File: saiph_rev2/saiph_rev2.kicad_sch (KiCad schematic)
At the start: 205 parts, among them SW1 SW_PUSH, SW10 SW_PUSH, SW100 SW_PUSH, SW101 SW_PUSH, SW102 SW_PUSH, SW103 SW_PUSH, SW104 SW_PUSH, SW105 SW_PUSH, SW109 SW_PUSH, SW11 SW_PUSH, SW110 SW_PUSH, SW111 SW_PUSH, SW12 SW_PUSH, SW13 SW_PUSH, SW14 SW_PUSH, SW15 SW_PUSH, SW16 SW_PUSH, SW17 SW_PUSH, SW18 SW_PUSH, SW19 SW_PUSH, SW2 SW_PUSH, SW20 SW_PUSH, SW21 SW_PUSH, SW22 SW_PUSH, SW23 SW_PUSH, SW24 SW_PUSH, SW25 SW_PUSH, SW26 SW_PUSH, SW27 SW_PUSH, SW28 SW_PUSH, SW29 SW_PUSH, SW3 SW_PUSH, SW30 SW_PUSH, SW31 SW_PUSH, SW32 SW_PUSH, SW33 SW_PUSH, SW34 SW_PUSH, SW35 SW_PUSH, SW36 SW_PUSH, SW37 SW_PUSH, SW38 SW_PUSH, SW39 SW_PUSH, SW4 SW_PUSH, SW40 SW_PUSH, SW41 SW_PUSH, SW42 SW_PUSH, SW43 SW_PUSH, SW44 SW_PUSH, SW45 SW_PUSH, SW46 SW_PUSH, SW47 SW_PUSH, SW48 SW_PUSH, SW49 SW_PUSH, SW5 SW_PUSH, SW50 SW_PUSH, SW51 SW_PUSH, SW52 SW_PUSH, SW53 SW_PUSH, SW54 SW_PUSH, SW55 SW_PUSH, SW56 SW_PUSH, SW57 SW_PUSH, SW58 SW_PUSH, SW59 SW_PUSH, SW6 SW_PUSH, SW60 SW_PUSH, SW61 SW_PUSH, SW62 SW_PUSH, SW63 SW_PUSH, SW64 SW_PUSH, SW65 SW_PUSH, SW66 SW_PUSH, SW67 SW_PUSH, SW68 SW_PUSH, SW69 SW_PUSH, SW7 SW_PUSH, SW70 SW_PUSH, SW71 SW_PUSH, SW72 SW_PUSH, SW73 SW_PUSH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

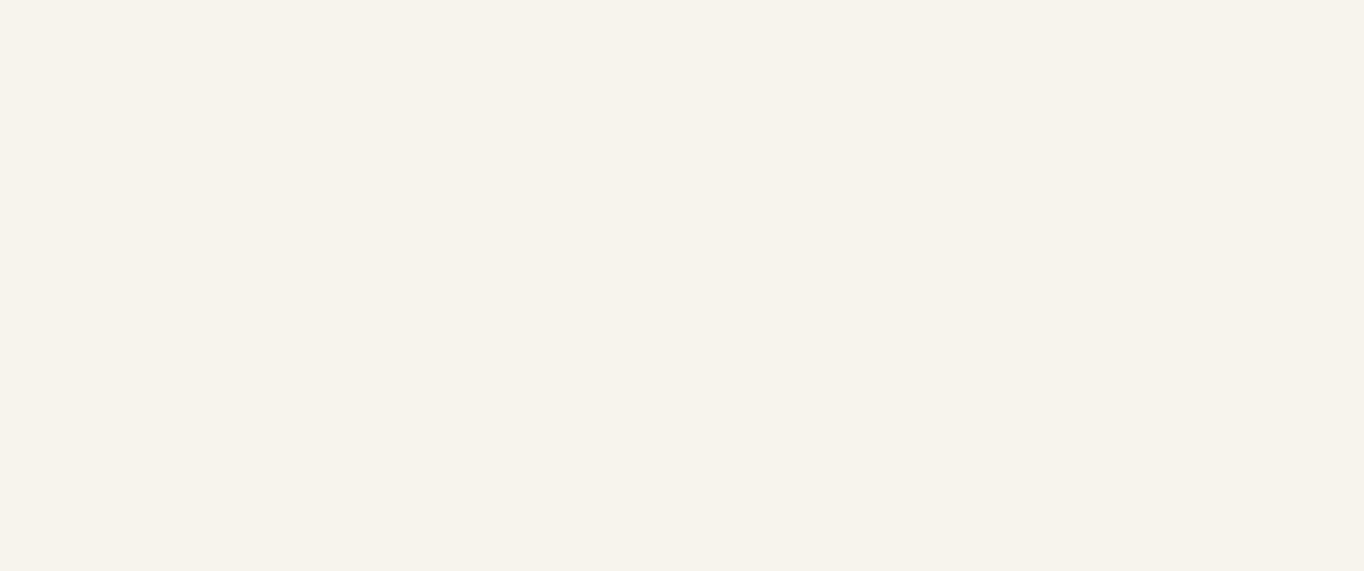
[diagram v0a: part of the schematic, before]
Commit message: add pro micro and usb
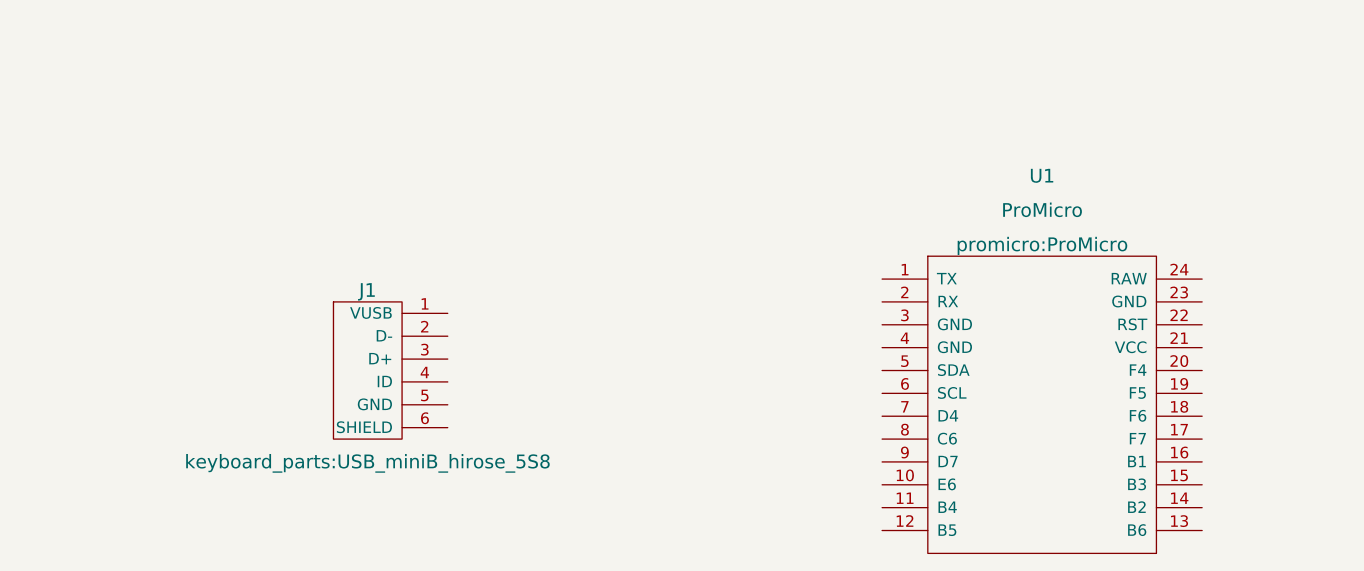
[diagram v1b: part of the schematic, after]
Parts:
- added J1: USB_mini_micro_B, keyboard_parts:USB_miniB_hirose_5S8, symbol keyboard_parts:USB_mini_micro_B
- added U1: ProMicro, promicro:ProMicro, symbol promicro:ProMicro
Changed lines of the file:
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@@
     (pin "2")
+  )
+  (symbol (lib_id "keyboard_parts:USB_mini_micro_B") (at 66.04 191.77 0) (unit 1)
+    (in_bom yes) (on_board yes)
+    (property "Reference" "J1" (id 0) (at 60.96 185.42 0)
+      (effects (font (size 1.524 1.524)))
+    )
+    (property "Value" "USB_mini_micro_B" (id 1) (at 62.23 185.42 0)
+      (effects (font (size 1.524 1.524)) hide)
+    )
+    (property "Footprint" "keyboard_parts:USB_miniB_hirose_5S8" (id 2) (at 60.96 204.47 0)
+      (effects (font (size 1.524 1.524)))
+    )
+    (property "Datasheet" "" (id 3) (at 64.77 191.77 0)
+      (effects (font (size 1.524 1.524)))
+    )
+    (pin "1")
+    (pin "2")
+    (pin "3")
+    (pin "4")
+    (pin "5")
+    (pin "6")
   )
   (symbol (lib_id "Device:LED") (at 26.67 31.75 0) (unit 1)
@@
     (pin "2")
   )
+  (symbol (lib_id "promicro:ProMicro") (at 135.89 203.2 0) (unit 1)
+    (in_bom yes) (on_board yes) (fields_autoplaced)
+    (property "Reference" "U1" (id 0) (at 135.89 172.72 0)
+      (effects (font (size 1.524 1.524)))
+    )
+    (property "Value" "ProMicro" (id 1) (at 135.89 176.53 0)
+      (effects (font (size 1.524 1.524)))
+    )
+    (property "Footprint" "promicro:ProMicro" (id 2) (at 135.89 180.34 0)
+      (effects (font (size 1.524 1.524)))
+    )
+    (property "Datasheet" "" (id 3) (at 138.43 229.87 0)
+      (effects (font (size 1.524 1.524)))
+    )
+    (pin "1")
+    (pin "10")
+    (pin "11")
+    (pin "12")
+    (pin "13")
+    (pin "14")
+    (pin "15")
+    (pin "16")
+    (pin "17")
+    (pin "18")
+    (pin "19")
+    (pin "2")
+    (pin "20")
+    (pin "21")
+    (pin "22")
+    (pin "23")
+    (pin "24")
+    (pin "3")
+    (pin "4")
+    (pin "5")
+    (pin "6")
+    (pin "7")
+    (pin "8")
+    (pin "9")
+  )
   (sheet_instances
     (path "/" (page "1"))
@@
       (reference "D98") (unit 1) (value "D") (footprint "Diodes_ThroughHole:D_DO-35_SOD27_P7.62mm_Horizontal")
     )
+    (path "/3b42597a-f840-489c-a144-f29527fd38e5"
+      (reference "J1") (unit 1) (value "USB_mini_micro_B") (footprint "keyboard_parts:USB_miniB_hirose_5S8")
+    )
     (path "/00000000-0000-0000-0000-000059446b96"
       (reference "SW1") (unit 1) (value "SW_PUSH") (footprint "keyboard_parts:ALPS_PLATE")
@@
       (reference "SW111") (unit 1) (value "SW_PUSH") (footprint "keyboard_parts:ALPS_PLATE_PLATE")
     )
+    (path "/d98210f0-6696-4934-86e8-c5c59831d86a"
+      (reference "U1") (unit 1) (value "ProMicro") (footprint "promicro:ProMicro")
+    )
   )

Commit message: add promicro
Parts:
- added J2: Conn_01x04, Connector_PinHeader_2.54mm:PinHeader_1x04_P2.54mm_Vertical, symbol Connector_Generic:Conn_01x04
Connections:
- net C0: now also U1.12 (B5)
- net C1: now also U1.11 (B4)
- net C2: now also U1.10 (E6)
- net C3: now also U1.9 (D7)
- net C4: now also U1.8 (C6)
- net C5: now also U1.7 (D4)
- net C6: now also U1.6 (SCL)
- net C7: now also U1.20 (F4)
- net C8: now also U1.19 (F5)
- net R0: now also U1.13 (B6)
- net R1: now also U1.14 (B2)
- net R2: now also U1.15 (B3)
- net R3: now also U1.16 (B1)
- net R4: now also U1.17 (F7)
- net R5: now also U1.18 (F6)
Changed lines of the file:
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@@
     (effects (font (size 1.27 1.27)) (justify left bottom))
+  )
+  (hierarchical_label "R0" (shape input) (at 153.67 212.09 0)
+    (effects (font (size 1.524 1.524)) (justify left))
   )
   (hierarchical_label "C0" (shape input) (at 110.49 33.02 90)
     (effects (font (size 1.524 1.524)) (justify left))
   )
+  (hierarchical_label "R3" (shape input) (at 153.67 204.47 0)
+    (effects (font (size 1.524 1.524)) (justify left))
+  )
+  (hierarchical_label "R2" (shape input) (at 153.67 207.01 0)
+    (effects (font (size 1.524 1.524)) (justify left))
+  )
   (hierarchical_label "C7" (shape input) (at 466.09 33.02 90)
     (effects (font (size 1.524 1.524)) (justify left))
   )
+  (hierarchical_label "C2" (shape input) (at 118.11 207.01 180)
+    (effects (font (size 1.524 1.524)) (justify right))
+  )
   (hierarchical_label "R0" (shape input) (at 109.22 45.72 180)
     (effects (font (size 1.524 1.524)) (justify right))
   )
+  (hierarchical_label "C3" (shape input) (at 118.11 204.47 180)
+    (effects (font (size 1.524 1.524)) (justify right))
+  )
   (hierarchical_label "C8" (shape input) (at 516.89 33.02 90)
     (effects (font (size 1.524 1.524)) (justify left))
   )
+  (hierarchical_label "C4" (shape input) (at 118.11 201.93 180)
+    (effects (font (size 1.524 1.524)) (justify right))
+  )
   (hierarchical_label "C2" (shape input) (at 210.82 33.02 90)
     (effects (font (size 1.524 1.524)) (justify left))
@@
     (effects (font (size 1.524 1.524)) (justify left))
   )
+  (hierarchical_label "C0" (shape input) (at 118.11 212.09 180)
+    (effects (font (size 1.524 1.524)) (justify right))
+  )
   (hierarchical_label "R5" (shape input) (at 109.22 134.62 180)
     (effects (font (size 1.524 1.524)) (justify right))
   )
+  (hierarchical_label "C6" (shape input) (at 118.11 196.85 180)
+    (effects (font (size 1.524 1.524)) (justify right))
+  )
+  (hierarchical_label "C7" (shape input) (at 153.67 194.31 0)
+    (effects (font (size 1.524 1.524)) (justify left))
+  )
   (hierarchical_label "R2" (shape input) (at 109.22 81.28 180)
     (effects (font (size 1.524 1.524)) (justify right))
   )
+  (hierarchical_label "R1" (shape input) (at 153.67 209.55 0)
+    (effects (font (size 1.524 1.524)) (justify left))
+  )
+  (hierarchical_label "C1" (shape input) (at 118.11 209.55 180)
+    (effects (font (size 1.524 1.524)) (justify right))
+  )
+  (hierarchical_label "R4" (shape input) (at 153.67 201.93 0)
+    (effects (font (size 1.524 1.524)) (justify left))
+  )
+  (hierarchical_label "R5" (shape input) (at 153.67 199.39 0)
+    (effects (font (size 1.524 1.524)) (justify left))
+  )
   (hierarchical_label "R4" (shape input) (at 109.22 116.84 180)
     (effects (font (size 1.524 1.524)) (justify right))
@@
     (effects (font (size 1.524 1.524)) (justify left))
   )
+  (hierarchical_label "C5" (shape input) (at 118.11 199.39 180)
+    (effects (font (size 1.524 1.524)) (justify right))
+  )
   (hierarchical_label "C5" (shape input) (at 364.49 33.02 90)
+    (effects (font (size 1.524 1.524)) (justify left))
+  )
+  (hierarchical_label "C8" (shape input) (at 153.67 196.85 0)
     (effects (font (size 1.524 1.524)) (justify left))
   )
@@
     (pin "1")
     (pin "2")
+  )
+  (symbol (lib_id "Connector_Generic:Conn_01x04") (at 81.28 193.04 0) (unit 1)
+    (in_bom yes) (on_board yes) (fields_autoplaced)
+    (property "Reference" "J2" (id 0) (at 83.82 193.0399 0)
+      (effects (font (size 1.27 1.27)) (justify left))
+    )
+    (property "Value" "Conn_01x04" (id 1) (at 83.82 195.5799 0)
+      (effects (font (size 1.27 1.27)) (justify left))
+    )
+    (property "Footprint" "Connector_PinHeader_2.54mm:PinHeader_1x04_P2.54mm_Vertical" (id 2) (at 81.28 193.04 0)
+      (effects (font (size 1.27 1.27)) hide)
+    )
+    (property "Datasheet" "~" (id 3) (at 81.28 193.04 0)
+      (effects (font (size 1.27 1.27)) hide)
+    )
+    (pin "1")
+    (pin "2")
+    (pin "3")
+    (pin "4")
   )
   (symbol (lib_id "keyboard_parts:USB_mini_micro_B") (at 66.04 191.77 0) (unit 1)
@@
       (reference "J1") (unit 1) (value "USB_mini_micro_B") (footprint "keyboard_parts:USB_miniB_hirose_5S8")
     )
+    (path "/11831a87-a89a-47da-93c1-04d31768f1fb"
+      (reference "J2") (unit 1) (value "Conn_01x04") (footprint "Connector_PinHeader_2.54mm:PinHeader_1x04_P2.54mm_Vertical")
+    )
     (path "/00000000-0000-0000-0000-000059446b96"

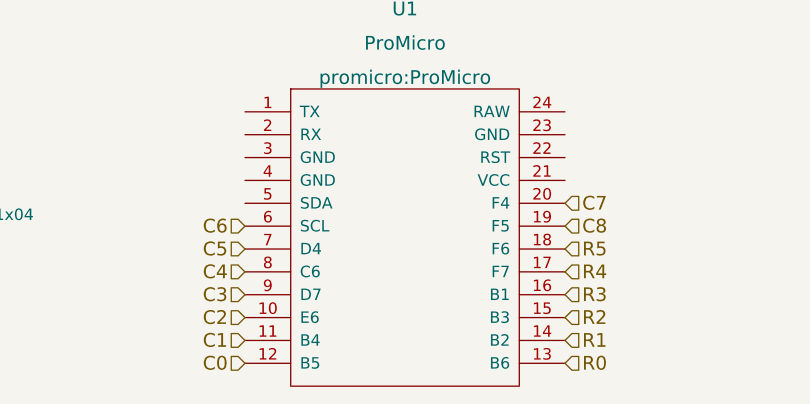
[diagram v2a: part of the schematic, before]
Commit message: change footprints to attempt better fit
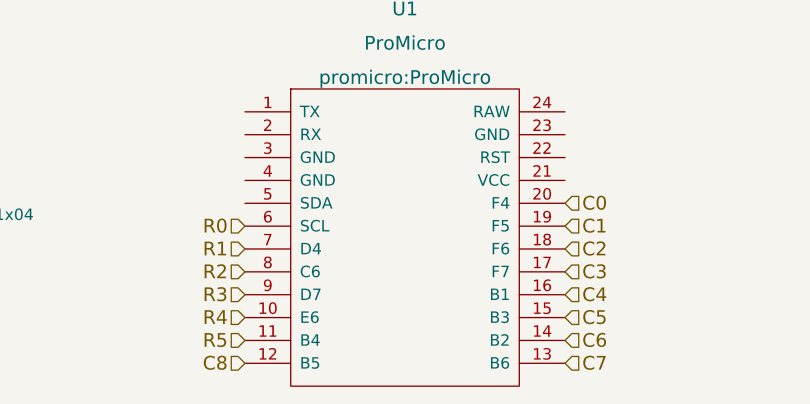
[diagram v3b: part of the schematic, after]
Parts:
- SW75, SW76, SW81, SW82: footprint keyboard_parts:ALPS_PLATE -> custom_parts:ALPS_PLATE_SPRING_PARTIAL
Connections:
- net C0: now also U1.20 (F4); no longer U1.12 (B5)
- net C1: now also U1.19 (F5); no longer U1.11 (B4)
- net C2: now also U1.18 (F6); no longer U1.10 (E6)
- net C3: now also U1.17 (F7); no longer U1.9 (D7)
- net C4: now also U1.16 (B1); no longer U1.8 (C6)
- net C5: now also U1.15 (B3); no longer U1.7 (D4)
- net C6: now also U1.14 (B2); no longer U1.6 (SCL)
- net C7: now also U1.13 (B6); no longer U1.20 (F4)
- net C8: now also U1.12 (B5); no longer U1.19 (F5)
- net R0: now also U1.6 (SCL); no longer U1.13 (B6)
- net R1: now also U1.7 (D4); no longer U1.14 (B2)
- net R2: now also U1.8 (C6); no longer U1.15 (B3)
- net R3: now also U1.9 (D7); no longer U1.16 (B1)
- net R4: now also U1.10 (E6); no longer U1.17 (F7)
- net R5: now also U1.11 (B4); no longer U1.18 (F6)
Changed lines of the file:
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@@
     (effects (font (size 1.27 1.27)) (justify left bottom))
   )
-  (hierarchical_label "R0" (shape input) (at 153.67 212.09 0)
-    (effects (font (size 1.524 1.524)) (justify left))
+  (hierarchical_label "R0" (shape input) (at 118.11 196.85 180)
+    (effects (font (size 1.524 1.524)) (justify right))
   )
   (hierarchical_label "C0" (shape input) (at 110.49 33.02 90)
     (effects (font (size 1.524 1.524)) (justify left))
   )
-  (hierarchical_label "R3" (shape input) (at 153.67 204.47 0)
-    (effects (font (size 1.524 1.524)) (justify left))
-  )
-  (hierarchical_label "R2" (shape input) (at 153.67 207.01 0)
-    (effects (font (size 1.524 1.524)) (justify left))
+  (hierarchical_label "R3" (shape input) (at 118.11 204.47 180)
+    (effects (font (size 1.524 1.524)) (justify right))
+  )
+  (hierarchical_label "R2" (shape input) (at 118.11 201.93 180)
+    (effects (font (size 1.524 1.524)) (justify right))
   )
   (hierarchical_label "C7" (shape input) (at 466.09 33.02 90)
     (effects (font (size 1.524 1.524)) (justify left))
   )
-  (hierarchical_label "C2" (shape input) (at 118.11 207.01 180)
-    (effects (font (size 1.524 1.524)) (justify right))
+  (hierarchical_label "C2" (shape input) (at 153.67 199.39 0)
+    (effects (font (size 1.524 1.524)) (justify left))
   )
   (hierarchical_label "R0" (shape input) (at 109.22 45.72 180)
     (effects (font (size 1.524 1.524)) (justify right))
   )
-  (hierarchical_label "C3" (shape input) (at 118.11 204.47 180)
-    (effects (font (size 1.524 1.524)) (justify right))
+  (hierarchical_label "C3" (shape input) (at 153.67 201.93 0)
+    (effects (font (size 1.524 1.524)) (justify left))
   )
   (hierarchical_label "C8" (shape input) (at 516.89 33.02 90)
     (effects (font (size 1.524 1.524)) (justify left))
   )
-  (hierarchical_label "C4" (shape input) (at 118.11 201.93 180)
-    (effects (font (size 1.524 1.524)) (justify right))
+  (hierarchical_label "C4" (shape input) (at 153.67 204.47 0)
+    (effects (font (size 1.524 1.524)) (justify left))
   )
   (hierarchical_label "C2" (shape input) (at 210.82 33.02 90)
@@
     (effects (font (size 1.524 1.524)) (justify left))
   )
-  (hierarchical_label "C0" (shape input) (at 118.11 212.09 180)
-    (effects (font (size 1.524 1.524)) (justify right))
+  (hierarchical_label "C0" (shape input) (at 153.67 194.31 0)
+    (effects (font (size 1.524 1.524)) (justify left))
   )
   (hierarchical_label "R5" (shape input) (at 109.22 134.62 180)
     (effects (font (size 1.524 1.524)) (justify right))
   )
-  (hierarchical_label "C6" (shape input) (at 118.11 196.85 180)
-    (effects (font (size 1.524 1.524)) (justify right))
-  )
-  (hierarchical_label "C7" (shape input) (at 153.67 194.31 0)
+  (hierarchical_label "C6" (shape input) (at 153.67 209.55 0)
+    (effects (font (size 1.524 1.524)) (justify left))
+  )
+  (hierarchical_label "C7" (shape input) (at 153.67 212.09 0)
     (effects (font (size 1.524 1.524)) (justify left))
   )
@@
     (effects (font (size 1.524 1.524)) (justify right))
   )
-  (hierarchical_label "R1" (shape input) (at 153.67 209.55 0)
+  (hierarchical_label "R1" (shape input) (at 118.11 199.39 180)
+    (effects (font (size 1.524 1.524)) (justify right))
+  )
+  (hierarchical_label "C1" (shape input) (at 153.67 196.85 0)
     (effects (font (size 1.524 1.524)) (justify left))
   )
-  (hierarchical_label "C1" (shape input) (at 118.11 209.55 180)
+  (hierarchical_label "R4" (shape input) (at 118.11 207.01 180)
     (effects (font (size 1.524 1.524)) (justify right))
   )
-  (hierarchical_label "R4" (shape input) (at 153.67 201.93 0)
-    (effects (font (size 1.524 1.524)) (justify left))
-  )
-  (hierarchical_label "R5" (shape input) (at 153.67 199.39 0)
-    (effects (font (size 1.524 1.524)) (justify left))
+  (hierarchical_label "R5" (shape input) (at 118.11 209.55 180)
+    (effects (font (size 1.524 1.524)) (justify right))
   )
   (hierarchical_label "R4" (shape input) (at 109.22 116.84 180)
@@
     (effects (font (size 1.524 1.524)) (justify left))
   )
-  (hierarchical_label "C5" (shape input) (at 118.11 199.39 180)
-    (effects (font (size 1.524 1.524)) (justify right))
+  (hierarchical_label "C5" (shape input) (at 153.67 207.01 0)
+    (effects (font (size 1.524 1.524)) (justify left))
   )
   (hierarchical_label "C5" (shape input) (at 364.49 33.02 90)
     (effects (font (size 1.524 1.524)) (justify left))
   )
-  (hierarchical_label "C8" (shape input) (at 153.67 196.85 0)
-    (effects (font (size 1.524 1.524)) (justify left))
+  (hierarchical_label "C8" (shape input) (at 118.11 212.09 180)
+    (effects (font (size 1.524 1.524)) (justify right))
   )
   (hierarchical_label "C3" (shape input) (at 262.89 33.02 90)
@@
     (property "Reference" "SW75" (id 0) (at 480.06 35.306 0))
     (property "Value" "SW_PUSH" (id 1) (at 476.25 40.132 0))
-    (property "Footprint" "keyboard_parts:ALPS_PLATE" (id 2) (at 476.25 38.1 0)
+    (property "Footprint" "custom_parts:ALPS_PLATE_SPRING_PARTIAL" (id 2) (at 476.25 38.1 0)
       (effects (font (size 1.27 1.27)) hide)
     )
@@
     (property "Reference" "SW81" (id 0) (at 505.46 35.306 0))
     (property "Value" "SW_PUSH" (id 1) (at 501.65 40.132 0))
-    (property "Footprint" "keyboard_parts:ALPS_PLATE" (id 2) (at 501.65 38.1 0)
+    (property "Footprint" "custom_parts:ALPS_PLATE_SPRING_PARTIAL" (id 2) (at 501.65 38.1 0)
       (effects (font (size 1.27 1.27)) hide)
     )
@@
     (property "Reference" "SW82" (id 0) (at 505.46 53.086 0))
     (property "Value" "SW_PUSH" (id 1) (at 501.65 57.912 0))
-    (property "Footprint" "keyboard_parts:ALPS_PLATE" (id 2) (at 501.65 55.88 0)
+    (property "Footprint" "custom_parts:ALPS_PLATE_SPRING_PARTIAL" (id 2) (at 501.65 55.88 0)
       (effects (font (size 1.27 1.27)) hide)
     )
@@
     (property "Reference" "SW76" (id 0) (at 480.06 53.086 0))
     (property "Value" "SW_PUSH" (id 1) (at 476.25 57.912 0))
-    (property "Footprint" "keyboard_parts:ALPS_PLATE" (id 2) (at 476.25 55.88 0)
+    (property "Footprint" "custom_parts:ALPS_PLATE_SPRING_PARTIAL" (id 2) (at 476.25 55.88 0)
       (effects (font (size 1.27 1.27)) hide)
     )
@@
     )
     (path "/00000000-0000-0000-0000-00005944d9e6"
-      (reference "SW75") (unit 1) (value "SW_PUSH") (footprint "keyboard_parts:ALPS_PLATE")
+      (reference "SW75") (unit 1) (value "SW_PUSH") (footprint "custom_parts:ALPS_PLATE_SPRING_PARTIAL")
     )
     (path "/00000000-0000-0000-0000-00005944ea98"
-      (reference "SW76") (unit 1) (value "SW_PUSH") (footprint "keyboard_parts:ALPS_PLATE")
+      (reference "SW76") (unit 1) (value "SW_PUSH") (footprint "custom_parts:ALPS_PLATE_SPRING_PARTIAL")
     )
     (path "/00000000-0000-0000-0000-000059451392"
@@
     )
     (path "/00000000-0000-0000-0000-00005944da2e"
-      (reference "SW81") (unit 1) (value "SW_PUSH") (footprint "keyboard_parts:ALPS_PLATE")
+      (reference "SW81") (unit 1) (value "SW_PUSH") (footprint "custom_parts:ALPS_PLATE_SPRING_PARTIAL")
     )
     (path "/00000000-0000-0000-0000-00005944da34"
-      (reference "SW82") (unit 1) (value "SW_PUSH") (footprint "keyboard_parts:ALPS_PLATE")
+      (reference "SW82") (unit 1) (value "SW_PUSH") (footprint "custom_parts:ALPS_PLATE_SPRING_PARTIAL")
     )
     (path "/00000000-0000-0000-0000-00005944da46"
